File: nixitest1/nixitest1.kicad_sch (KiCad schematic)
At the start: 32 parts, among them J1 MSYS, Q1 60V 3A, Q10 HVN, Q11 HVN, Q12 HVN, Q13 HVN, Q2 HVN, Q3 HVN, Q4 HVN, Q5 HVN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

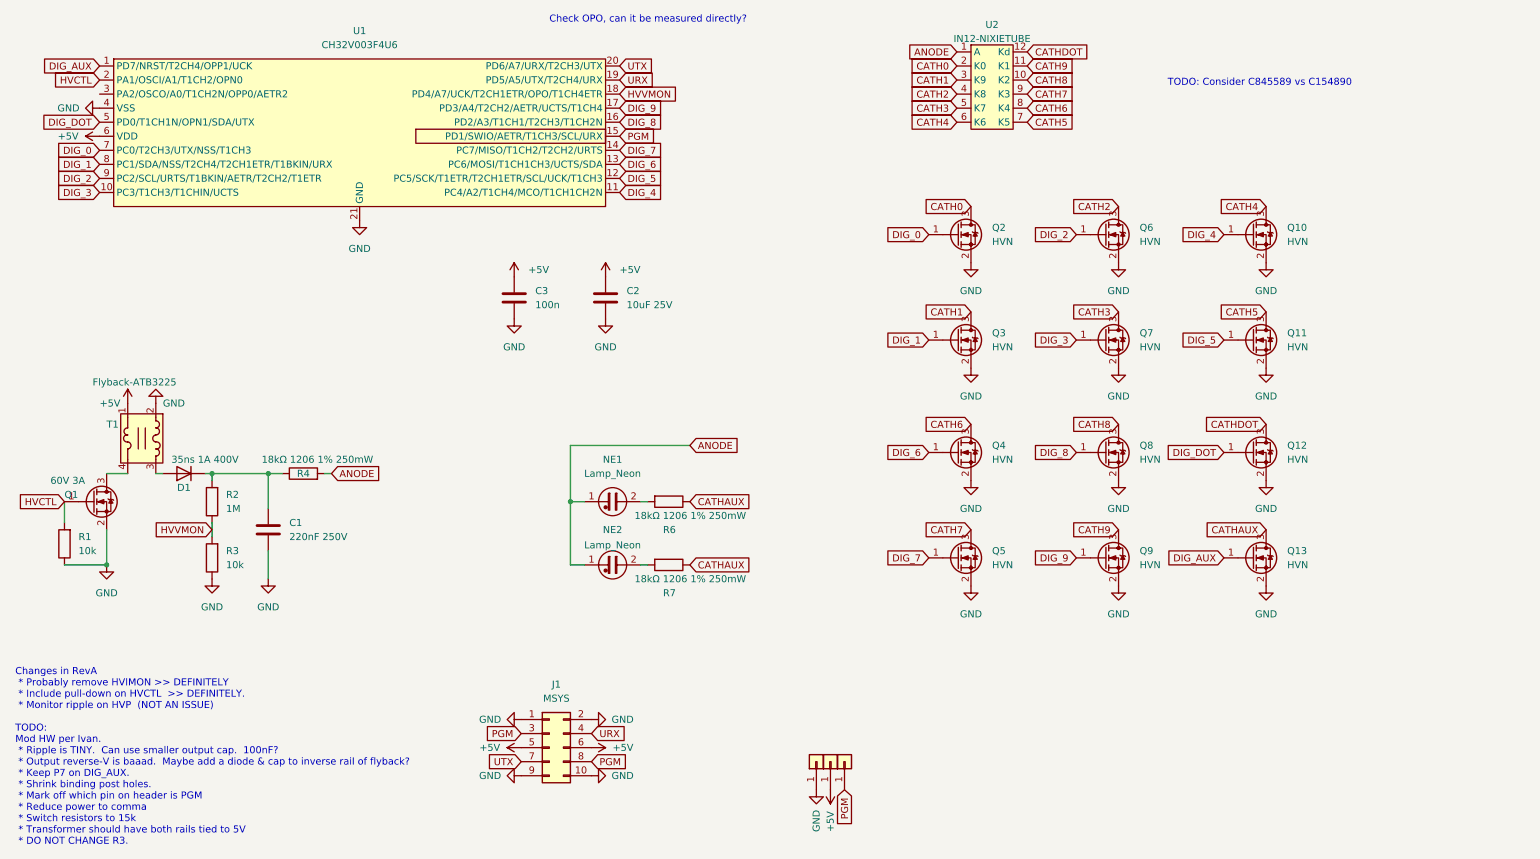
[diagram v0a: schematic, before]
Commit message: Update design based on tests of first rev.
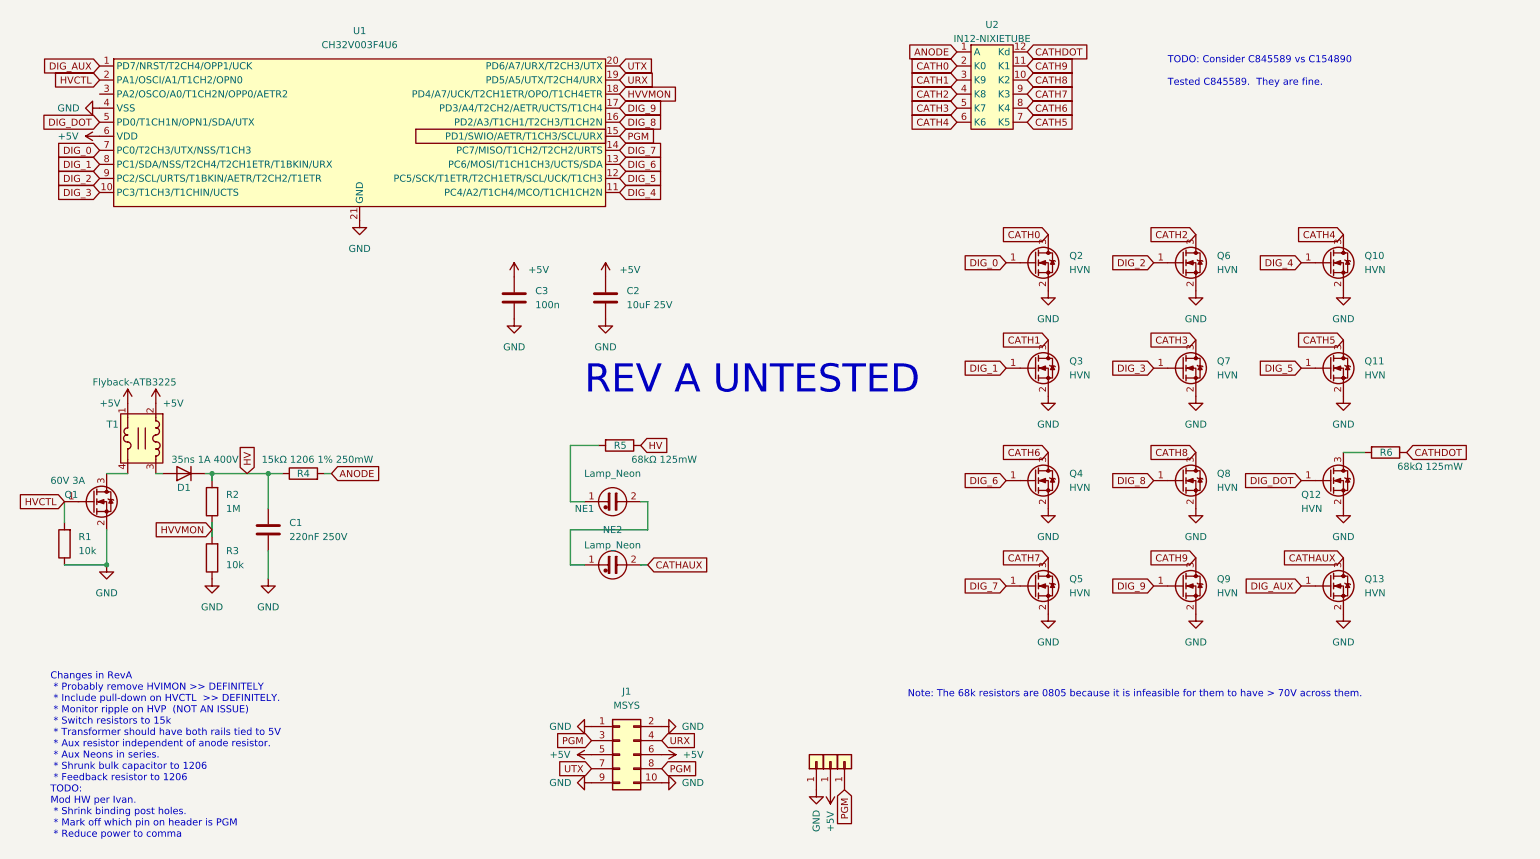
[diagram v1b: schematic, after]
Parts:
- removed R7: 18kΩ 1206 1% 250mW, Resistor_SMD:R_1206_3216Metric, symbol Device:R
- added R5: 68kΩ 125mW, Resistor_SMD:R_0805_2012Metric, symbol Device:R
- C1: footprint Capacitor_SMD:C_1210_3225Metric -> Capacitor_SMD:C_1206_3216Metric; LCSC C326671 -> C377089
- R2: footprint Resistor_SMD:R_0805_2012Metric -> Resistor_SMD:R_1206_3216Metric; LCSC C131391 -> C108083
- R4: value 18kΩ 1206 1% 250mW -> 15kΩ 1206 1% 250mW; LCSC C229367 -> C114932
- R6: value 18kΩ 1206 1% 250mW -> 68kΩ 125mW; footprint Resistor_SMD:R_1206_3216Metric -> Resistor_SMD:R_0805_2012Metric; LCSC C229367 -> C114548
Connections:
- net +5V: now also T1.2
- net ANODE: no longer NE1.1, NE2.1
- net CATHAUX: now also NE2.2; no longer R6.1
- net CATHDOT: now also R6.1; no longer Q12.3 (D)
- net GND: no longer T1.2
- net HV: now reaches C1.1, D1.1 (K), R2.2, R4.1
- net HV: now also R5.1
- net at NE1.2: now also NE2.1; no longer R6.2
- new net: Q12.3 (D), R6.2
- new net: NE1.1, R5.2
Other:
- note added: "Changes in RevA * Probably remove HVIMON >> DEFINITELY * Include pull-down on HVCTL >> DEFINITELY. * Monitor ripple on HVP (NOT AN ISSUE) * Switch resistors to 15k * Transformer should have both rails tied to 5V * Aux resistor independent of anode resistor. * Aux Neons in series. * Shrunk bulk capacitor to 1206 * Feedback resistor to 1206 TODO: Mod HW per Ivan. * Shrink binding post holes. * Mark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"
- note added: "Note: The 68k resistors are 0805 because it is infeasible for them to have > 70V across them."
- note added: "REV A UNTESTED"
- note added: "TODO: Consider C845589 vs C154890 Tested C845589. They are fine."
- note removed: "Changes in RevA * Probably remove HVIMON >> DEFINITELY * Include pull-down on HVCTL >> DEFINITELY. * Monitor ripple on HVP (NOT AN ISSUE) TODO: Mod HW per Ivan. * Ripple is TINY. Can use smaller output cap. 100nF? * Output reverse-V is baaad. Maybe add a diode & cap to inverse rail of flyback? * Keep P7 on DIG_AUX. * Shrink binding post holes. * Mark off which pin on header is PGM * Reduce power 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"
- note removed: "Check OPO, can it be measured directly?"
- note removed: "TODO: Consider C845589 vs C154890"
- moved on the sheet: J1, Q10, Q11, Q12, Q13, Q2, Q3, Q4, Q5, Q6, Q7, Q8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
